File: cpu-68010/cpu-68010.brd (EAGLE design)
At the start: 150 x 100 mm, 47 parts, among them IC10 74HC30D, IC11 74HC30D, IC12 74HC85D, IC13 MAX232, IC6 74HC00D, IC7 74HCT154DW, IC8 74HC04D, IC9 74HC148D, X1 FABC96R

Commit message: removed multifunction peripheral; to be replaced with 68564
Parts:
- removed IC2: (no value), 68komputer:PLCC52-S
- removed R1: 10k, rcl:R2012
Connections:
- net RS232_RX renamed RS232_0_RX
- net RS232_TX renamed RS232_0_TX
- removed net !68901_CS: IC2.52, IC6.3
- removed net !68901_DTACK: IC10.1, IC2.50, R1.1
- removed net !68901_IACK: IC2.49
- removed net !68901_IRQ: IC2.36, IC9.3
- removed net GPIO0: IC2.25
- removed net GPIO1: IC2.26
- removed net GPIO2: IC2.27
- removed net GPIO3: IC2.28
- removed net GPIO4: IC2.29
- removed net GPIO5: IC2.30
- removed net GPIO6: IC2.31
- removed net GPIO7: IC2.32
- removed net UART_CLK: IC2.11, IC2.8
- removed net UART_RX: IC13.12, IC2.10
- removed net UART_TX: IC13.11, IC2.9
- new net !68564_CS: IC6.3
- new net !68564_DTACK: IC10.2
- new net !68564_IRQ: IC9.3
- new net UART0_RX: IC13.12
- new net UART0_TX: IC13.11
- net !EXT_DTACK: now also IC10.1; no longer IC10.2
- net !LDS: no longer IC2.51
- net !RESET: no longer IC2.24
- net +5V: no longer IC2.12, R1.2
- net A1: no longer IC2.3
- net A2: no longer IC2.4
- net A3: no longer IC2.5
- net A4: no longer IC2.6
- net A5: no longer IC2.7
- net CLK: no longer IC2.19, IC2.39
- net D0: no longer IC2.41
- net D1: no longer IC2.42
- net D2: no longer IC2.43
- net D3: no longer IC2.45
- net D4: no longer IC2.44
- net D5: no longer IC2.46
- net D6: no longer IC2.47
- net D7: no longer IC2.48
- net GND: no longer IC2.38, IC2.40
- net R!W!: no longer IC2.2

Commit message: added 68681 DUART
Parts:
- added C31, C32: 30pF, rcl:C0805
- added IC2: (no value), 68komputer:PLCC-S44
- added LED1, LED2, LED3, LED4, LED5, LED6, LED7, LED8: GRN, led:CHIPLED_1206
- added Q1: 3.6864MHz, crystal:HC49/S
- added R1, R10, R11, R2, R3, R4, R5, R6: 680R, rcl:M0805
- added X3: (no value), con-subd:F09HP
- moved IC5 98.0 mm to (66.2, 56.3)
- moved C12 67.0 mm to (22.2, 77.3), turned to 90 degrees
- moved QG1 9.70 mm to (116.2, 16.9)
- moved IC4 0.27 mm to (68.9, 34.2), turned to 0 degrees
- moved IC3 0.24 mm to (68.9, 11.8), turned to 0 degrees
- moved IC1 0.19 mm to (114.9, 50.0)
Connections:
- removed net !68564_CS: IC6.3
- removed net !68564_DTACK: IC10.2
- removed net !68564_IRQ: IC9.3
- new net !68681_CS: IC2.39, IC6.3
- new net !68681_DTACK: IC10.2, IC2.10
- new net !68681_IRQ: IC2.24, IC9.3
- new net !68681_IRQACK: IC2.41
- new net 68681_XTAL1: C31.1, IC2.36, Q1.2
- new net 68681_XTAL2: C32.2, IC2.37, Q1.1
- new net GPIO_IN0: IC2.8
- new net GPIO_IN1: IC2.5
- new net GPIO_IN2: IC2.40
- new net GPIO_IN3: IC2.3
- new net GPIO_IN4: IC2.43
- new net GPIO_IN5: IC2.42
- new net GPIO_OUT0: IC2.32, R4.1
- new net GPIO_OUT1: IC2.14, R3.1
- new net GPIO_OUT2: IC2.31, R2.1
- new net GPIO_OUT3: IC2.15, R1.1
- new net GPIO_OUT4: IC2.30, R11.1
- new net GPIO_OUT5: IC2.16, R10.1
- new net GPIO_OUT6: IC2.29, R6.1
- new net GPIO_OUT7: IC2.17, R5.1
- new net N$10: LED1.A, R1.2
- new net N$11: LED2.A, R2.2
- new net N$12: LED1.C, LED2.C
- new net N$13: LED5.A, R3.2
- new net N$14: LED6.A, R4.2
- new net N$15: LED3.C, LED4.C, LED5.C, LED6.C, LED7.C, LED8.C
- new net N$16: LED7.A, R5.2
- new net N$17: LED8.A, R6.2
- new net N$7: LED3.A, R10.2
- new net N$8: LED4.A, R11.2
- new net RS232_1_RX: IC13.7, X3.2
- new net RS232_1_TX: IC13.8, X3.3
- new net UART1_RX: IC13.9, IC2.11
- new net UART1_TX: IC13.10, IC2.13
- net !RESET: now also IC2.38
- net +5V: now also IC2.44
- net A1: now also IC2.2
- net A2: now also IC2.4
- net A3: now also IC2.6
- net A4: now also IC2.7
- net D0: now also IC2.28
- net D1: now also IC2.18
- net D2: now also IC2.27
- net D3: now also IC2.19
- net D4: now also IC2.26
- net D5: now also IC2.20
- net D6: now also IC2.25
- net D7: now also IC2.21
- net GND: now also C31.2, C32.1, IC2.22, X3.5, X3.G1, X3.G2
- net R!W!: now also IC2.9
- net UART0_RX: now also IC2.35
- net UART0_TX: now also IC2.33
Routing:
- net RS232_1_RX: track 0.00 -> 54.1 mm
- net RS232_1_TX: track 0.00 -> 53.6 mm
- net +5V: track 0.00 -> 3.22 mm
- net N$5: track 19.5 -> 18.1 mm

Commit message: added RAM to board, moved some stuff around
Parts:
- added C33, C35, C36, C37, C38, C39, C40: 100nF, rcl:C0805
- added C34: 47µF, rcl:CT6032
- added IC14, IC15, IC16, IC17: (no value), 68komputer:SO32X
- added LED9: GRN, led:CHIPLED_1206
- added R12, R7, R8, R9: 10k, rcl:M0805
- added R13: 680R, rcl:M0805
- added S1, S2: (no value), switch-omron:B3F-10XX
- IC12: value 74HC85D -> 74HC14D; device 74xx-eu:SO16 -> 74xx-eu:SO14
- moved IC9 198.9 mm to (129.3, 80.0)
- moved IC11 180.7 mm to (122.1, 25.2), turned to 180 degrees
- moved IC8 159.8 mm to (96.9, 82.2)
- moved IC10 153.5 mm to (90.7, 93.0), turned to 180 degrees
- moved IC12 145.7 mm to (128.3, 9.45), turned to 90 degrees
- moved IC7 134.6 mm to (112.6, 84.1), turned to 180 degrees
- moved IC6 66.3 mm to (33.5, 47.9)
- moved X3 42.1 mm to (32.9, 88.2), turned to 0 degrees
- moved C32 38.4 mm to (-56.4, 35.4)
- moved R11 35.7 mm to (-59.1, 27.1)
- moved R6 33.3 mm to (-48.2, 22.9)
- moved C31 28.2 mm to (-50.0, 28.3)
- moved R2 19.8 mm to (-53.3, 14.9)
- moved C28 19.8 mm to (37.7, 70.1), turned to 90 degrees
- moved LED2 19.7 mm to (-65.5, 14.0)
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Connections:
- removed net !ROM_WE: IC3.31, IC4.31
- new net !A18: IC14.30, IC15.30, IC16.30, IC17.30, IC8.10
- new net !TIMER_IRQ: IC9.3
- new net N$18: R7.2, S1.1, S1.2
- new net N$19: LED9.A, R13.2
- new net N$9: R8.2, S2.1, S2.2
- new net NMI_SW: C37.1, IC12.13, R12.1, R7.1
- new net R/!W!: IC14.29, IC15.29, IC16.29, IC17.29, IC3.31, IC4.31
- new net RESET_SW: C38.1, IC12.9, R8.1, R9.1
- net !68681_IRQ: now also IC9.2; no longer IC9.3
- net !NMI: now also IC12.12
- net !OE: now also IC14.24, IC15.24, IC16.24, IC17.24
- net !REGION1: now also IC14.22, IC15.22, IC16.22, IC17.22
- net !RESET: now also IC12.8
- net +5V: now also C33.1, C34.+, C35.1, C36.1, C39.1, C40.1, IC12.14, IC14.32, IC15.32, IC16.32, IC17.32, R13.1, S1.3, S1.4, S2.3, S2.4; no longer IC12.16, IC9.2
- net A1: now also IC14.12, IC15.12, IC16.12, IC17.12
- net A10: now also IC14.26, IC15.26, IC16.26, IC17.26
- net A11: now also IC14.23, IC15.23, IC16.23, IC17.23
- net A12: now also IC14.25, IC15.25, IC16.25, IC17.25
- net A13: now also IC14.4, IC15.4, IC16.4, IC17.4
- net A14: now also IC14.28, IC15.28, IC16.28, IC17.28
- net A15: now also IC14.3, IC15.3, IC16.3, IC17.3
- net A16: now also IC14.31, IC15.31, IC16.31, IC17.31
- net A17: now also IC14.2, IC15.2, IC16.2, IC17.2
- net A18: now also IC8.11
- net A2: now also IC14.11, IC15.11, IC16.11, IC17.11
- net A3: now also IC14.10, IC15.10, IC16.10, IC17.10
- net A4: now also IC14.9, IC15.9, IC16.9, IC17.9
- net A5: now also IC14.8, IC15.8, IC16.8, IC17.8
- net A6: now also IC14.7, IC15.7, IC16.7, IC17.7
- net A7: now also IC14.6, IC15.6, IC16.6, IC17.6
- net A8: now also IC14.5, IC15.5, IC16.5, IC17.5
- net A9: now also IC14.27, IC15.27, IC16.27, IC17.27
- net D0: now also IC15.13, IC17.13
- net D1: now also IC15.14, IC17.14
- net D10: now also IC14.15, IC16.15
- net D11: now also IC14.17, IC16.17
- net D12: now also IC14.18, IC16.18
- net D13: now also IC14.19, IC16.19
- net D14: now also IC14.20, IC16.20
- net D15: now also IC14.21, IC16.21
- net D2: now also IC15.15, IC17.15
- net D3: now also IC15.17, IC17.17
- net D4: now also IC15.18, IC17.18
- net D5: now also IC15.19, IC17.19
- net D6: now also IC15.20, IC17.20
- net D7: now also IC15.21, IC17.21
- net D8: now also IC14.13, IC16.13
- net D9: now also IC14.14, IC16.14
- net GND: now also C33.2, C34.-, C35.2, C36.2, C37.2, C38.2, C39.2, C40.2, IC12.7, IC14.16, IC15.16, IC16.16, IC17.16, LED9.C, R12.2, R9.2; no longer IC12.8
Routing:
- net +5V: track 3.22 -> 43.7 mm, vias 0 -> 1
- net RS232_1_TX: track 53.6 -> 19.3 mm
- net RS232_1_RX: track 54.1 -> 19.7 mm
- net RS232_0_TX: track 6.03 -> 21.7 mm
- net N$9: track 0.00 -> 14.3 mm
- net N$18: track 0.00 -> 13.5 mm
- net RS232_0_RX: track 5.83 -> 18.3 mm
- net RESET_SW: track 0.00 -> 7.95 mm
- net NMI_SW: track 0.00 -> 7.91 mm
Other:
- board text added: "!NMI"
- board text added: "!RESET"
- board text added: "High ROM"
- board text added: "Low ROM"

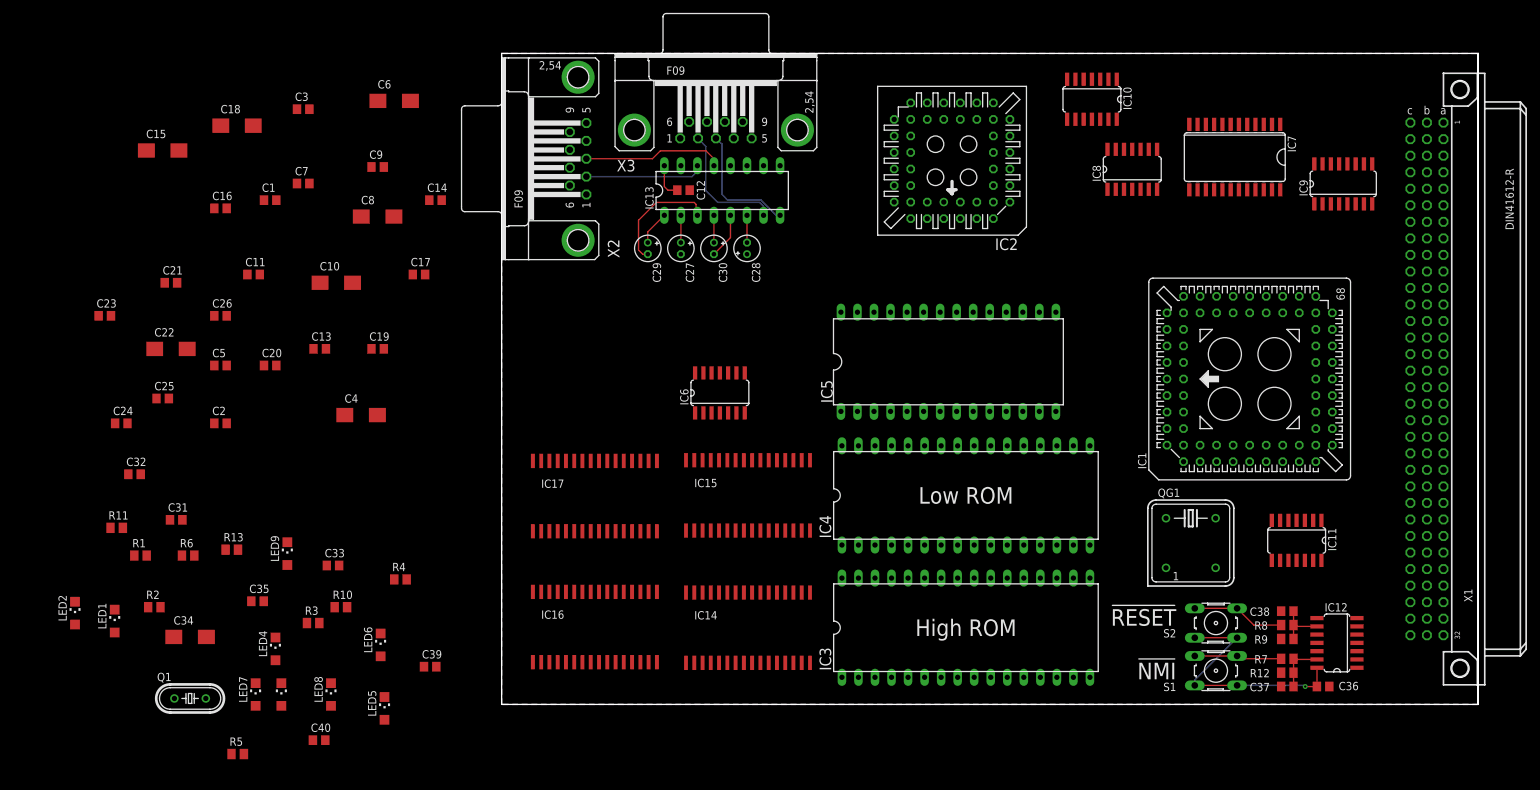
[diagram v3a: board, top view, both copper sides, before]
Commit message: routed address/data between banks of RAM/ROM
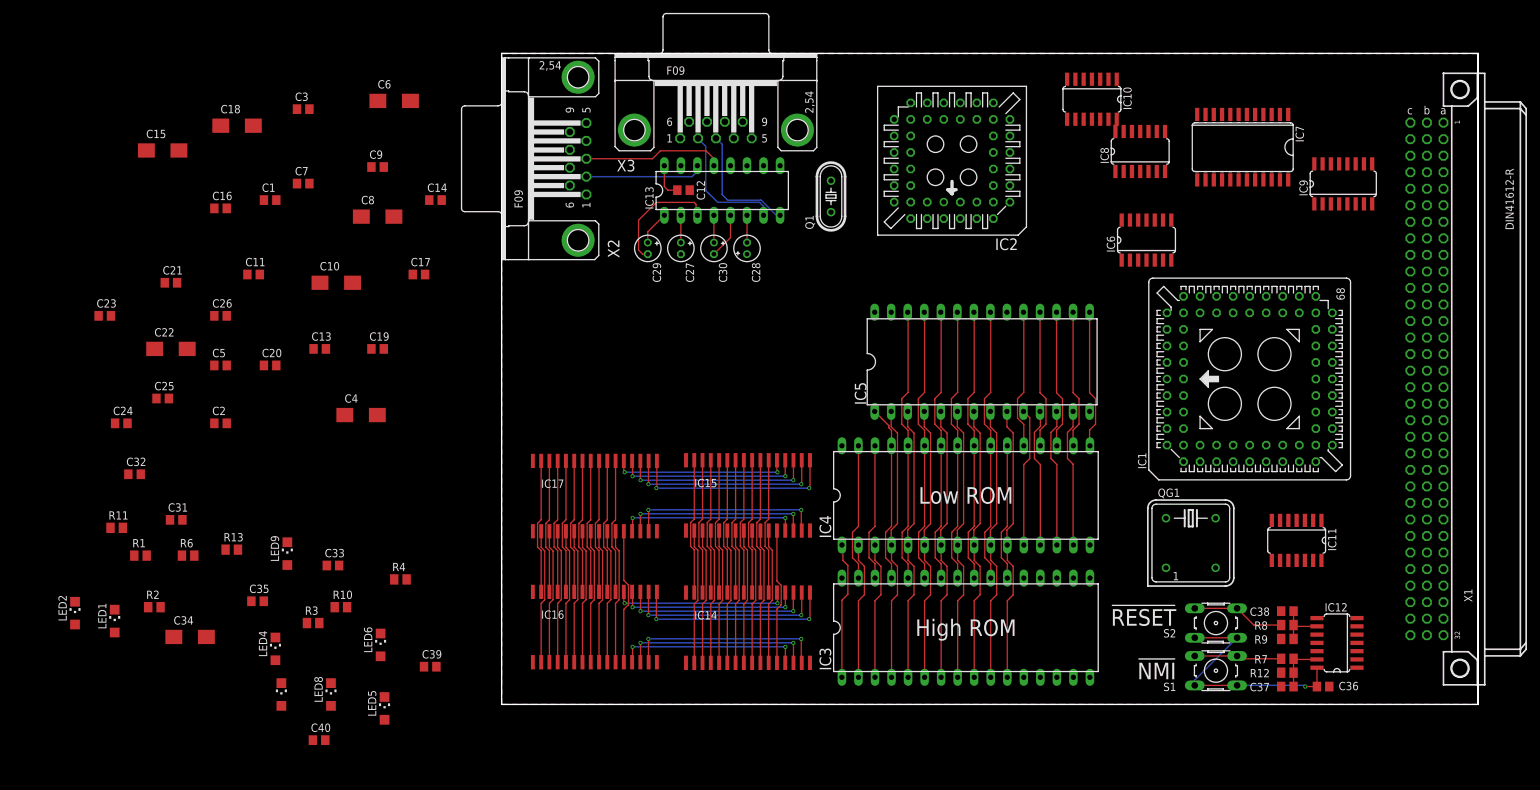
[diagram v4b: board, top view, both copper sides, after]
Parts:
- removed LED7: GRN, led:CHIPLED_1206
- removed R5: 680R, rcl:M0805
- moved Q1 125.1 mm to (50.6, 78.0), turned to 90 degrees
- moved IC6 69.6 mm to (99.1, 71.3)
- moved IC5 5.18 mm to (73.8, 52.6)
- moved IC8 3.00 mm to (98.1, 84.9)
- moved IC7 1.95 mm to (113.8, 85.6)
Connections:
- removed net GPIO_OUT7: IC2.17, R5.1
- removed net N$12: LED1.C, LED2.C
- removed net N$15: LED3.C, LED4.C, LED5.C, LED6.C, LED7.C, LED8.C
- removed net N$16: LED7.A, R5.2
- new net TIMER_CLK: IC2.31
- net GND: now also LED6.C, LED8.C
- net GPIO_OUT2: now also IC2.15; no longer IC2.31
- net GPIO_OUT3: now also IC2.30; no longer IC2.15
- net GPIO_OUT4: now also IC2.16; no longer IC2.30
- net GPIO_OUT5: now also IC2.29; no longer IC2.16
- net GPIO_OUT6: now also IC2.17; no longer IC2.29
- net R!W!: no longer IC2.9, IC5.27
- net R/!W!: now also IC2.9, IC5.27
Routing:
- net A8: track 0.00 -> 84.2 mm
- net A5: track 0.00 -> 83.9 mm
- net A3: track 0.00 -> 83.9 mm
- net A2: track 0.00 -> 83.9 mm
- net A6: track 0.00 -> 83.9 mm
- net A9: track 0.00 -> 83.8 mm
- net A13: track 0.00 -> 83.8 mm
- net A12: track 0.00 -> 83.8 mm
- net A7: track 0.00 -> 83.8 mm
- net A4: track 0.00 -> 83.8 mm
- net A14: track 0.00 -> 83.8 mm
- net A10: track 0.00 -> 83.8 mm
- net !OE: track 0.00 -> 83.8 mm
- net A11: track 0.00 -> 83.8 mm
- net A15: track 0.00 -> 68.8 mm
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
